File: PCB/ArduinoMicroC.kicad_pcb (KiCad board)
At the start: 4 copper layers, 18 x 36.2 mm, 28 parts, among them J1 USB_C_Receptacle_USB2.0, J2 Conn_01x12, J3 Conn_01x06, J4 Conn_01x12, SW1 SW_Check_USB, SW2 SW_Push, U1 MIC5219-5.0YM5, U2 ATmega32U4-MU, Y1 16MHz

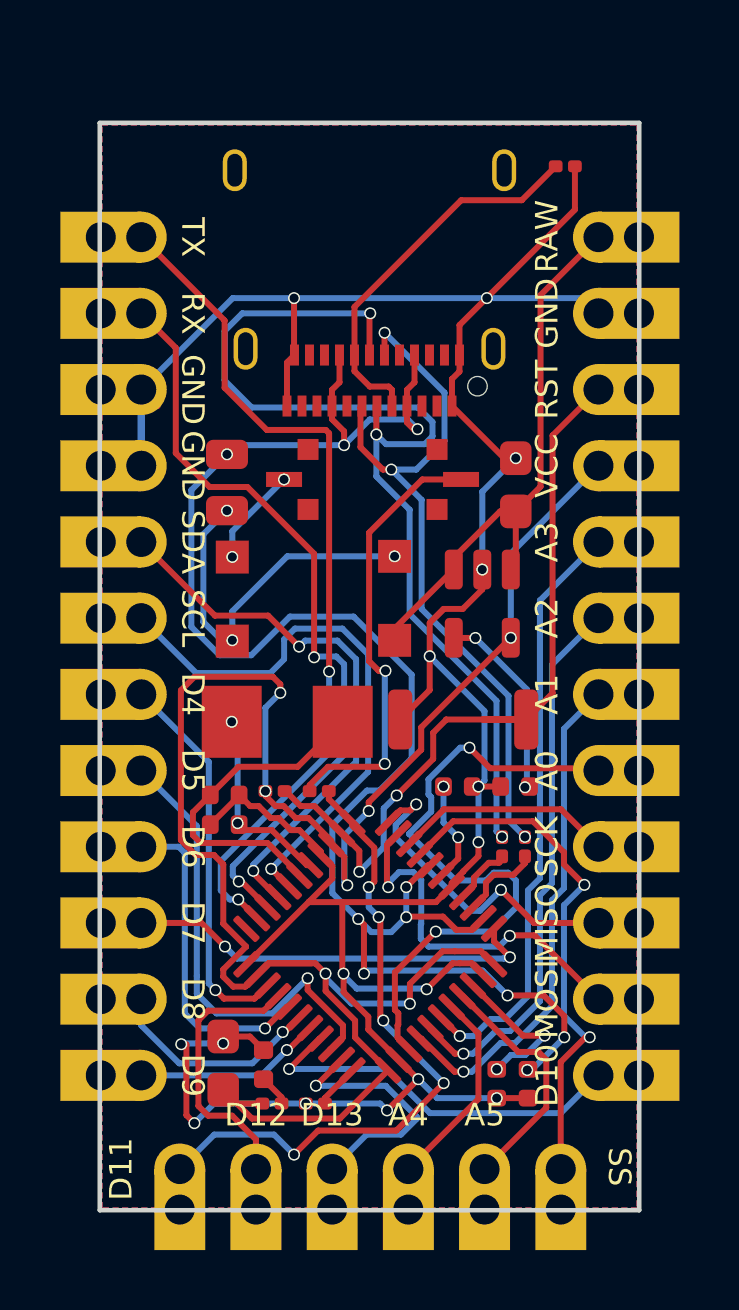
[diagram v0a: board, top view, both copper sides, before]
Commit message: Second version of PCB
- Make D11 pin is USB check pin only.
- Remove D11 out of GPIO headers.
- Remove TX LED and RX LED.
- Smaller PCB with 29 pins instead of 30 pins.
- Fix the USB check diode.
- Add a Resistor to GND in D11 pin.
- Use USB-C 2.0 connector instead of 3.0.
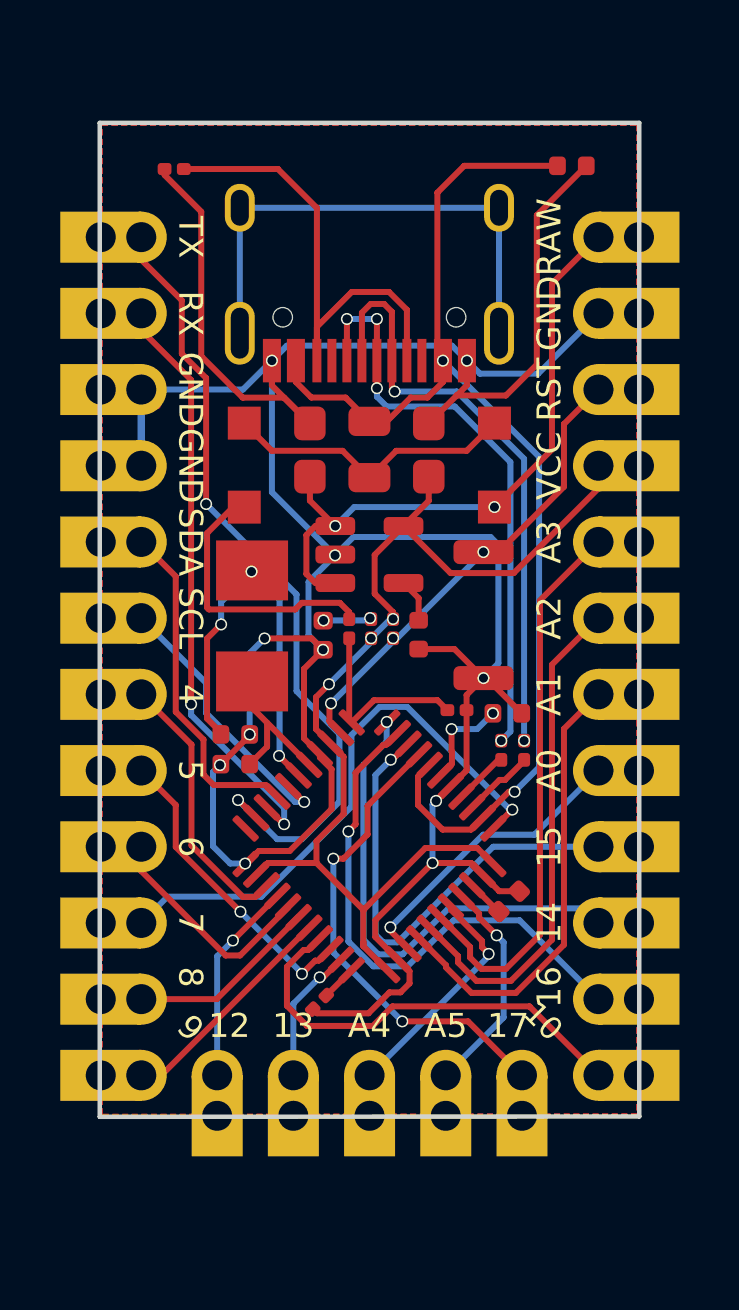
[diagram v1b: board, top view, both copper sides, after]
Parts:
- removed SW1: SW_Check_USB, Button_Switch_SMD:SW_DIP_SPSTx01_Slide_Copal_CVS-01xB_W5.9mm_P1mm
- added R7: 1K, Resistor_SMD:R_0201_0603Metric, F.Cu at (144.2, 92.5)
- J1: footprint Connector_USB:USB_C_Receptacle_Amphenol_12401610E4-2A -> Connector_USB:USB_C_Receptacle_HRO_TYPE-C-31-M-12
- J3: value Conn_01x06 -> Conn_01x05; footprint NeihConnector:PinHeader_1x06_P2.54mm_Circular_Vertical_2 -> NeihConnector:PinHeader_1x05_P2.54mm_Circular_Vertical_2
- R10: value 1K -> 10K
- U2: value ATmega32U4-MU -> ATmega32U4-M; footprint NeihPackage:QFN-44-1EP_7x7mm_P0.5mm_EP5.2x5.2mm -> Package_DFN_QFN:QFN-44-1EP_7x7mm_P0.5mm_EP5.2x5.2mm
- moved C8 30.6 mm to (148.0, 74.3), turned to 0 degrees
- moved C3 21.6 mm to (143.3, 83.8)
- moved R4 16.2 mm to (141.3, 89.8), turned to 90 degrees
- moved D2 14.5 mm to (139.7, 90.0), turned to 90 degrees
- moved R3 13.0 mm to (134.8, 74.4), turned to 180 degrees
- moved C1 6.96 mm to (139.3, 83.8)
- moved R5 6.70 mm to (142.1, 89.8), turned to 270 degrees
- moved C6 6.09 mm to (145.9, 98.8), turned to 225 degrees
- moved C2 6.00 mm to (142.9, 90.0), turned to 270 degrees
- moved D3 5.55 mm to (145.4, 84.3)
- moved R10 5.50 mm to (140.6, 89.8), turned to 90 degrees
- moved F1 4.87 mm to (141.3, 83.8)
- moved D1 4.48 mm to (137.1, 84.3)
- moved U1 4.10 mm to (141.3, 87.3), turned to 0 degrees
- moved SW2 3.54 mm to (145.1, 89.3), turned to 270 degrees
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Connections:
- net D10 renamed 10
- net D4 renamed 4
- net D5 renamed 5
- net D6 renamed 6
- net D7 renamed 7
- net D8 renamed 8
- net D9 renamed 9
- net MISO renamed 14
- net MOSI renamed 16
- net SCK renamed 15
- D3 pad 2: Net-(D1-Pad1) -> Net-(D1-Pad2)
- F1 pad 2: Net-(D1-Pad1) -> Net-(D1-Pad2)
- J3 pad 1: D11 -> 12
- J3 pad 2: D12 -> 13
- J3 pad 3: D13 -> A4
- J3 pad 4: A4 -> A5
- J3 pad 5: A5 -> 17
- R10 pad 1: D11 -> 11
- R10 pad 2: Net-(R10-Pad2) -> Net-(D1-Pad1)
- U2 pad 12: D11 -> 11
- U2 pad 26: D12 -> 12
- U2 pad 32: D13 -> 13
- U2 pad 8: SS -> 17
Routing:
- net VCC: track 66.8 -> 39.5 mm, vias 7 -> 3
- net D11: track 23.0 -> 0.00 mm, vias 5 -> 0
- net SS: track 18.7 -> 0.00 mm, vias 2 -> 0
- net VBUS: track 56.9 -> 39.1 mm, vias 10 -> 2
- net Net-(J1-PadS1): track 0.00 -> 17.0 mm
- net 17: track 0.00 -> 16.0 mm, vias 0 -> 2
- net Net-(R10-Pad2): track 14.9 -> 0.00 mm, vias 2 -> 0
- net Net-(J1-PadA6): track 34.5 -> 19.7 mm, vias 3 -> 4
- net GND: track 106.1 -> 117.6 mm, vias 16 -> 11
- net A0: track 22.8 -> 11.4 mm, vias 2 -> 1
- net RESET: track 26.4 -> 15.7 mm, vias 2 -> 3
- net SCL: track 20.0 -> 9.31 mm
- net A3: track 29.0 -> 18.6 mm, vias 1 -> 0
- net D12: track 9.40 -> 0.00 mm
- net D13: track 8.59 -> 0.00 mm, vias 1 -> 0
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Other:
- board size 18 x 36.2 mm -> 18 x 33.1 mm
- board text added: "10"
- board text added: "12"
- board text added: "13"
- board text added: "14"
- board text added: "15"
- board text added: "16"
- board text added: "17"
- board text added: "4"
- board text added: "5"
- board text added: "6"
- board text added: "7"
- board text added: "8"
- board text added: "9"
- board text removed: "D10"
- board text removed: "D11"
- board text removed: "D12"
- board text removed: "D13"
- board text removed: "D4"
- board text removed: "D5"
- board text removed: "D6"
- board text removed: "D7"
- board text removed: "D8"
- board text removed: "D9"
- board text removed: "MISO"
- board text removed: "MOSI"
- board text removed: "SCK"
- board text removed: "SS"

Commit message: Make zone outline for USB Sheld and update module library and footprint for new version
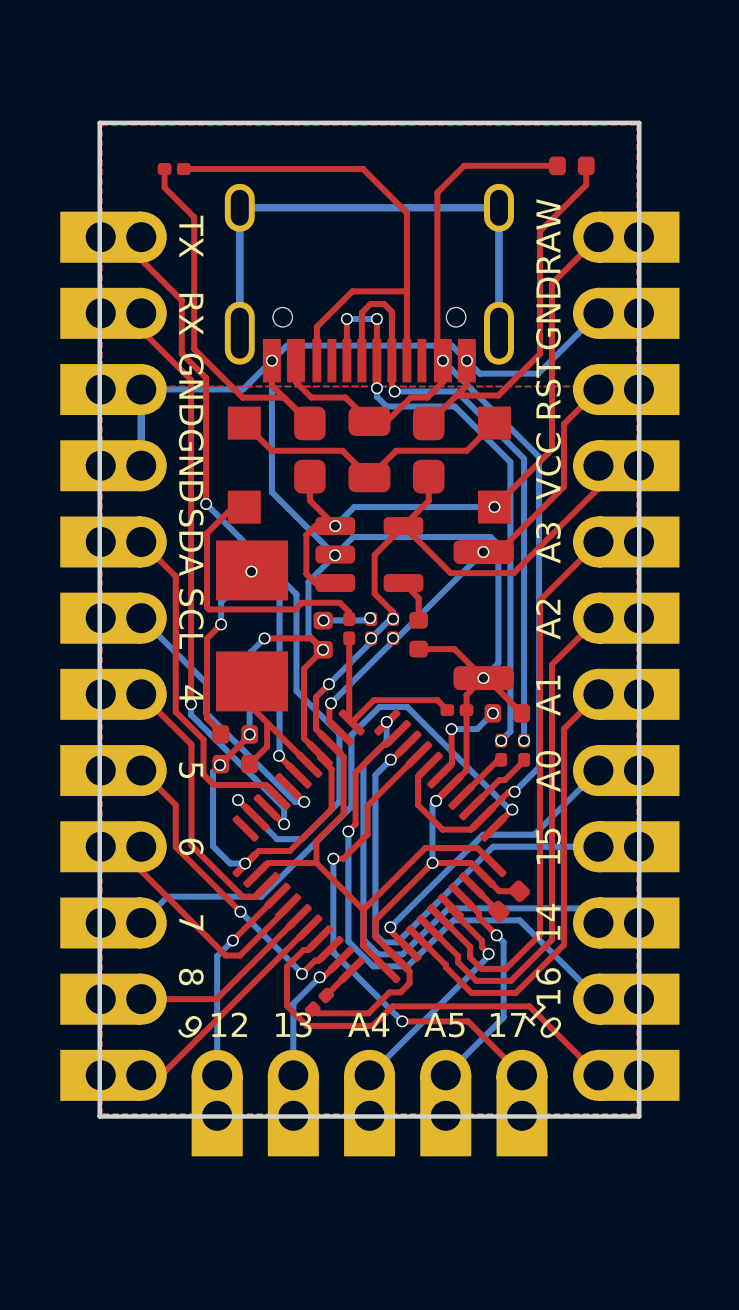
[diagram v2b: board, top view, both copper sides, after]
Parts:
- R4: value 1K -> 10K
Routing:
- net Net-(J1-PadA5): track 16.6 -> 17.6 mm
- added copper zone on B.Cu, net Net-(J1-PadS1)
- added copper zone on F.Cu, net Net-(J1-PadS1)
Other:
- copper layers 4 -> 2

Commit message: Update Schematic for version 3
Add D+ and D- pins for headers
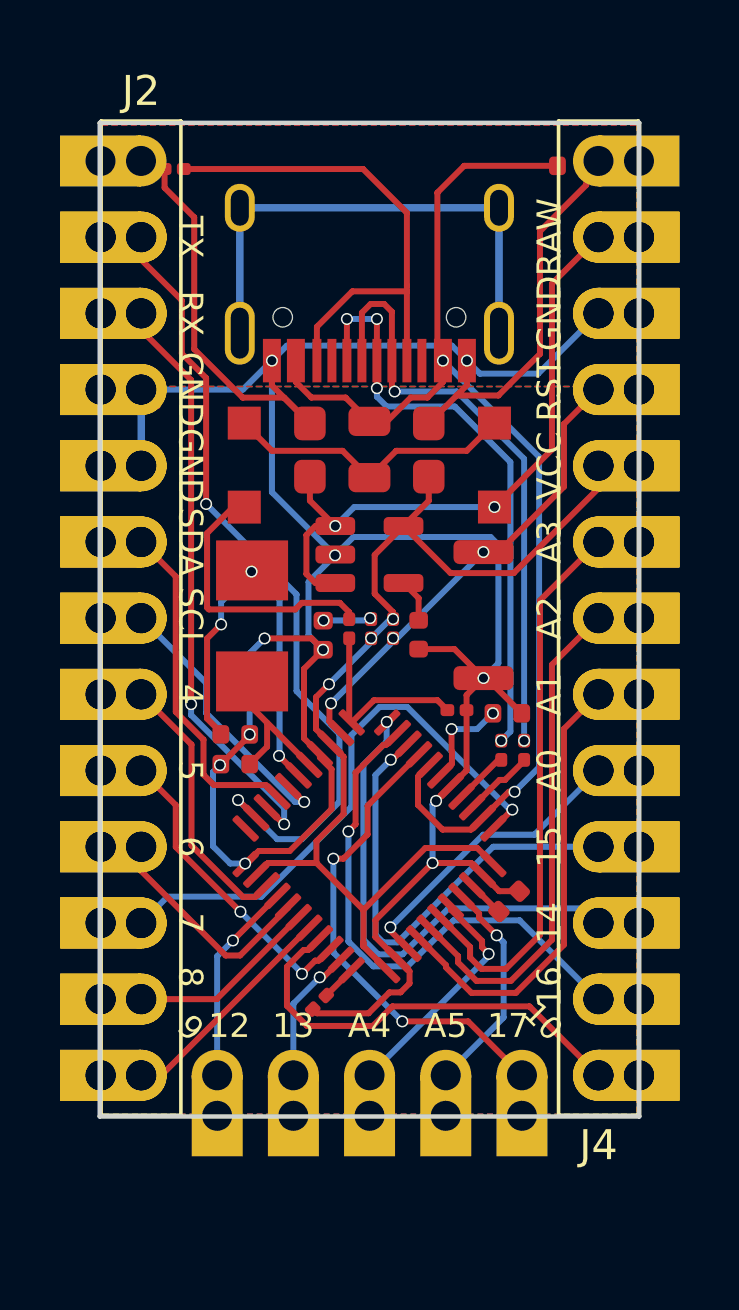
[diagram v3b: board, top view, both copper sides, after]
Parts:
- added J2: Conn_01x13, NeihConnector:PinHeader_1x13_P2.54mm_Circular_Vertical_2, F.Cu at (133.7, 74.2)
- added J4: Conn_01x13, NeihConnector:PinHeader_1x13_P2.54mm_Circular_Vertical_2, F.Cu at (148.9, 104.6)
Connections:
- J1 pad A6: Net-(J1-PadA6) -> D+
- J1 pad A7: Net-(J1-PadA7) -> D-
- J1 pad B6: Net-(J1-PadA6) -> D+
- J1 pad B7: Net-(J1-PadA7) -> D-
- R1 pad 1: Net-(J1-PadA6) -> D+
- R1 pad 2: D+ -> C_D+
- R2 pad 1: Net-(J1-PadA7) -> D-
- R2 pad 2: D- -> C_D-
- U2 pad 3: D- -> C_D-
- U2 pad 4: D+ -> C_D+
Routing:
- net Net-(J1-PadA7): track 20.2 -> 0.00 mm, vias 2 -> 0
- net Net-(J1-PadA6): track 19.7 -> 0.00 mm, vias 4 -> 0
- net D+: track 1.83 -> 19.7 mm, vias 0 -> 4
- net D-: track 2.41 -> 20.2 mm, vias 0 -> 2
- net C_D-: track 0.00 -> 2.41 mm
- net C_D+: track 0.00 -> 1.83 mm

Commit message: Update device modules in PCB for version 3
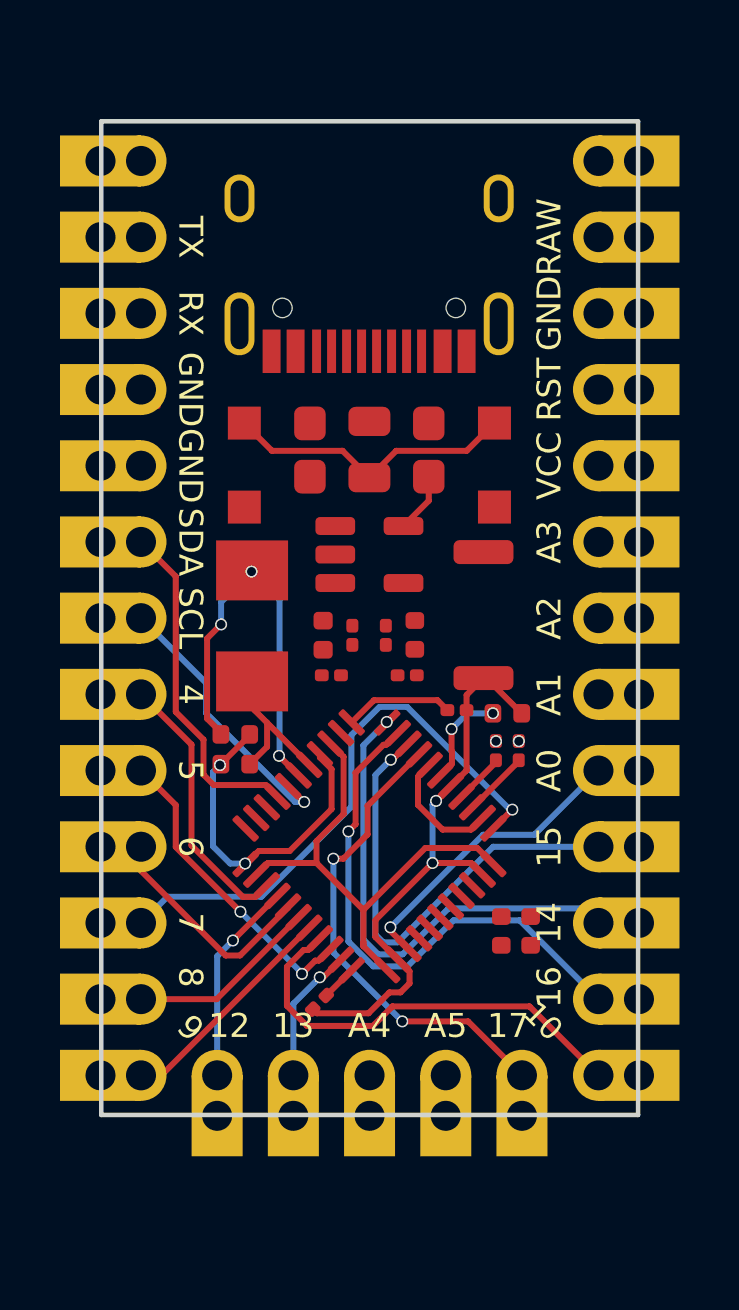
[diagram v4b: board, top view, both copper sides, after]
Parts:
- removed the J2 at (133.7, 76.7)
- removed the J4 at (148.9, 104.6)
- moved C8 25.5 mm to (146.6, 99.8), turned to 270 degrees
- moved R3 18.6 mm to (142.5, 91.3)
- moved R5 2.58 mm to (140.0, 91.3), turned to 0 degrees
- moved C6 1.02 mm to (145.7, 99.8), turned to 270 degrees
- moved R4 0.54 mm to (141.8, 90.0)
- moved J1 0.31 mm to (141.3, 76.5)
- moved R10 0.24 mm to (140.7, 90.0)
- moved R1 0.18 mm to (145.5, 93.8)
- moved R2 0.18 mm to (146.3, 93.8)
- moved C2 0.13 mm to (142.8, 90.0)
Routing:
- net GND: track 117.4 -> 32.1 mm, vias 11 -> 4
- net VBUS: track 39.1 -> 4.16 mm, vias 2 -> 0
- net TX: track 27.8 -> 0.00 mm, vias 2 -> 0
- net RAW: track 22.5 -> 0.00 mm, vias 2 -> 0
- net RX: track 20.8 -> 0.00 mm, vias 2 -> 0
- net VCC: track 39.5 -> 19.3 mm, vias 3 -> 0
- net D-: track 20.2 -> 0.00 mm, vias 2 -> 1
- net D+: track 19.7 -> 0.00 mm, vias 4 -> 1
- net A3: track 18.6 -> 0.00 mm
- net Net-(J1-PadA5): track 17.6 -> 0.00 mm
- net Net-(J1-PadS1): track 17.0 -> 0.00 mm
- net A2: track 16.9 -> 0.00 mm
- net RESET: track 15.7 -> 0.00 mm, vias 3 -> 0
- net A1: track 15.1 -> 0.00 mm
- net Net-(D1-Pad1): track 9.30 -> 0.00 mm
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- removed copper zone on B.Cu, net GND
- removed copper zone on F.Cu, net GND
- removed copper zone on B.Cu, net Net-(J1-PadS1)
- removed copper zone on F.Cu, net Net-(J1-PadS1)
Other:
- board size 18 x 33.1 mm -> 17.9 x 33.1 mm

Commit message: Update PCB for version 3
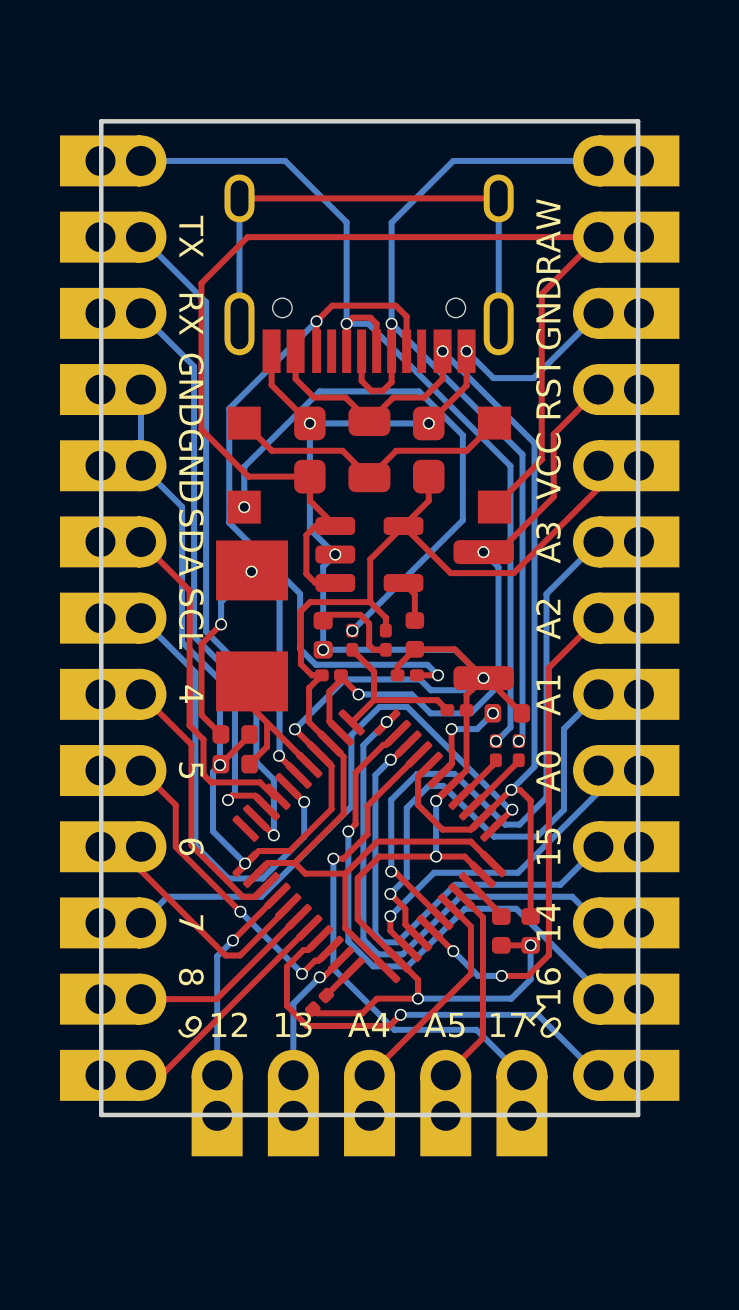
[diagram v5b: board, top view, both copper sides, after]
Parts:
- R4: value 10K -> 1K
- moved R10 0.17 mm to (140.7, 90.1)
- moved R4 0.17 mm to (141.8, 90.1), turned to 270 degrees
- turned C6 to 90 degrees
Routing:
- net GND: track 32.1 -> 95.3 mm, vias 4 -> 13
- net RAW: track 0.00 -> 38.9 mm
- net D-: track 0.00 -> 31.1 mm, vias 1 -> 2
- net D+: track 0.00 -> 30.9 mm, vias 1 -> 2
- net VBUS: track 4.16 -> 34.3 mm, vias 0 -> 2
- net Net-(J1-PadA5): track 0.00 -> 24.3 mm, vias 0 -> 2
- net TX: track 0.00 -> 22.6 mm, vias 0 -> 1
- net VCC: track 19.3 -> 41.1 mm
- net A3: track 0.00 -> 20.5 mm, vias 0 -> 1
- net RESET: track 0.00 -> 20.4 mm, vias 0 -> 2
- net RX: track 0.00 -> 19.1 mm, vias 0 -> 1
- net Net-(D1-Pad1): track 0.00 -> 18.3 mm, vias 0 -> 2
- net Net-(J1-PadS1): track 0.00 -> 17.0 mm
- net A2: track 0.00 -> 16.8 mm, vias 0 -> 2
- net A1: track 0.00 -> 15.9 mm, vias 0 -> 1
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
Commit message: Update Text for PCB
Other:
- board text added: "D+"
- board text added: "D-"

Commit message: Add filled zones for PCB
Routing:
- added copper zone on B.Cu, net (none)
- added copper zone on F.Cu, net (none)
- added copper zone on B.Cu, net Net-(J1-PadS1)
- added copper zone on F.Cu, net Net-(J1-PadS1)

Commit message: Update header J2, J4 and update filled zones
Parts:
- J2, J4: footprint NeihConnector:PinHeader_1x13_P2.54mm_Circular_Vertical_2 -> NeihConnector:PinHeader_1x13_P2.54mm_Circular_Vertical_3
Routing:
- net GND: track 95.3 -> 98.2 mm
- net D+: track 30.9 -> 32.8 mm
- net 9: track 7.64 -> 9.53 mm
- net D-: track 31.1 -> 33.0 mm
- net 10: track 15.5 -> 17.4 mm
- net TX: track 22.6 -> 23.5 mm
- net SDA: track 11.4 -> 12.3 mm
- net SCL: track 14.9 -> 15.9 mm
- net RX: track 19.1 -> 20.1 mm
- net 8: track 6.38 -> 7.33 mm
- net 7: track 19.5 -> 20.5 mm
- net 6: track 7.57 -> 8.52 mm
- net 5: track 10.3 -> 11.2 mm
- net 4: track 9.11 -> 10.1 mm
- net A5: track 6.72 -> 7.66 mm
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- added copper zone on B.Cu, net GND
- added copper zone on F.Cu, net GND
- removed copper zone on B.Cu, net (none)
- removed copper zone on F.Cu, net (none)
